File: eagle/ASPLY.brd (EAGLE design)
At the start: 118 x 89 mm, 69 parts, among them IC1 MC78L05ABP, IC2 TINY45, K1 Light, K2 Fan1, K3 Fan2, K4 Fan3, P1 MOLEX, T1 2SC1815, T2 2SC1815, T3 2SC1815, T4 2SC1815

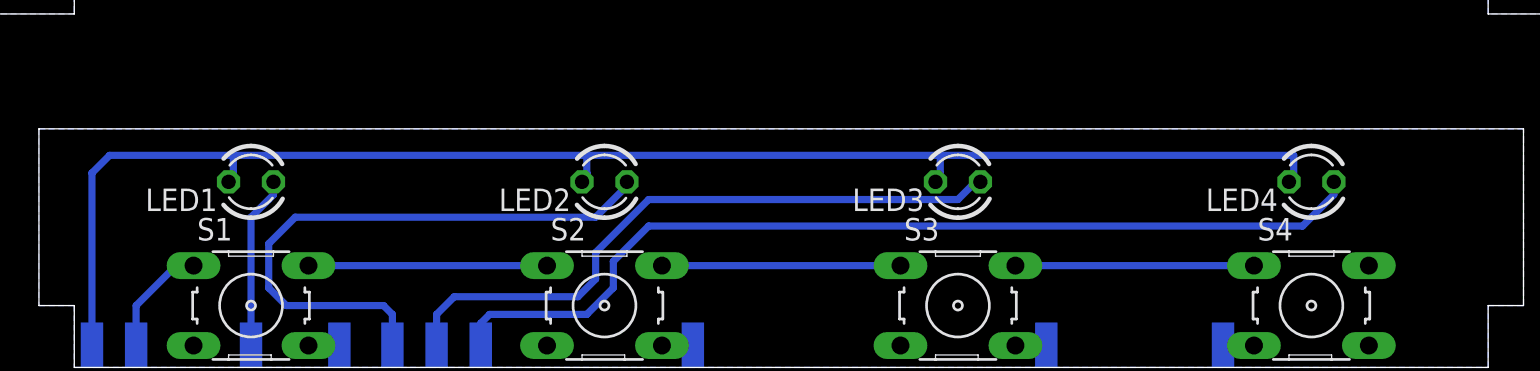
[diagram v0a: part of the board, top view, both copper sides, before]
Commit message: fix schema
The connection of emitter and collector are fixed. Increase in current
limiting resistors of transistors from 2 to 10 kOm
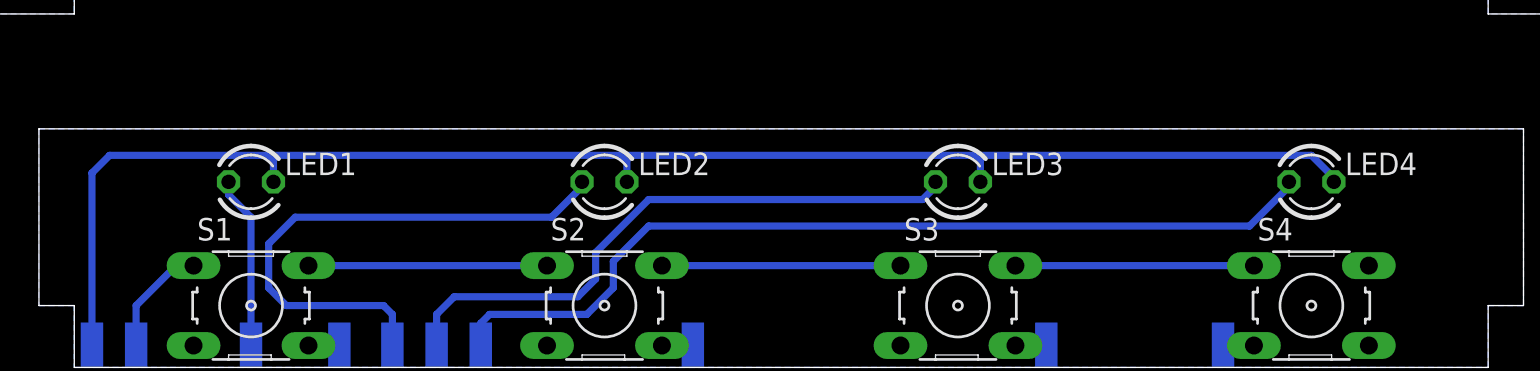
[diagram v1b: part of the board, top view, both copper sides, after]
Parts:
- turned LED1 to 0 degrees
- turned LED2 to 0 degrees
- turned LED3 to 0 degrees
- turned LED4 to 0 degrees
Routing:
- net N$25: track 54.4 -> 51.6 mm
- net N$27: track 33.7 -> 31.2 mm
- net N$26: track 36.5 -> 34.1 mm
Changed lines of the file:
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@@
 <layer number="17" name="Pads" color="2" fill="1" visible="yes" active="yes"/>
 <layer number="18" name="Vias" color="2" fill="1" visible="no" active="yes"/>
-<layer number="19" name="Unrouted" color="6" fill="1" visible="no" active="yes"/>
+<layer number="19" name="Unrouted" color="6" fill="1" visible="yes" active="yes"/>
 <layer number="20" name="Dimension" color="15" fill="1" visible="yes" active="yes"/>
 <layer number="21" name="tPlace" color="7" fill="1" visible="yes" active="yes"/>
 <layer number="22" name="bPlace" color="7" fill="1" visible="no" active="yes"/>
-<layer number="23" name="tOrigins" color="15" fill="1" visible="no" active="yes"/>
+<layer number="23" name="tOrigins" color="15" fill="1" visible="yes" active="yes"/>
 <layer number="24" name="bOrigins" color="15" fill="1" visible="no" active="yes"/>
-<layer number="25" name="tNames" color="7" fill="1" visible="yes" active="yes"/>
+<layer number="25" name="tNames" color="7" fill="1" visible="no" active="yes"/>
 <layer number="26" name="bNames" color="7" fill="1" visible="no" active="yes"/>
-<layer number="27" name="tValues" color="7" fill="1" visible="yes" active="yes"/>
+<layer number="27" name="tValues" color="7" fill="1" visible="no" active="yes"/>
 <layer number="28" name="bValues" color="7" fill="1" visible="no" active="yes"/>
 <layer number="29" name="tStop" color="7" fill="3" visible="no" active="yes"/>
@@
 <layer number="48" name="Document" color="7" fill="1" visible="no" active="yes"/>
 <layer number="49" name="Reference" color="7" fill="1" visible="no" active="yes"/>
-<layer number="51" name="tDocu" color="7" fill="1" visible="yes" active="yes"/>
+<layer number="51" name="tDocu" color="7" fill="1" visible="no" active="yes"/>
 <layer number="52" name="bDocu" color="7" fill="1" visible="no" active="yes"/>
 <layer number="91" name="Nets" color="2" fill="1" visible="no" active="no"/>
@@
 <attribute name="VALUE" x="65.365" y="17.54" size="1.27" layer="27" rot="R90"/>
 </element>
-<element name="LED1" library="led" package="LED3MM" value="Red" x="29" y="-9.5" rot="R180"/>
-<element name="LED2" library="led" package="LED3MM" value="Green" x="49" y="-9.5" rot="R180"/>
-<element name="LED3" library="led" package="LED3MM" value="Green" x="69" y="-9.5" rot="R180"/>
-<element name="LED4" library="led" package="LED3MM" value="Green" x="89" y="-9.5" rot="R180"/>
+<element name="LED1" library="led" package="LED3MM" value="Red" x="29" y="-9.5"/>
+<element name="LED2" library="led" package="LED3MM" value="Green" x="49" y="-9.5"/>
+<element name="LED3" library="led" package="LED3MM" value="Green" x="69" y="-9.5"/>
+<element name="LED4" library="led" package="LED3MM" value="Green" x="89" y="-9.5"/>
 <element name="S1" library="switch-omron" package="B3F-10XX" value="Light" x="29" y="-16.5" smashed="yes">
 <attribute name="OC_NEWARK" value="36M3542" x="29" y="-16.5" size="1.778" layer="27" display="off"/>
@@
 <contactref element="LED4" pad="A"/>
 <contactref element="U$14" pad="P$1"/>
-<wire x1="90.27" y1="-9.5" x2="90.27" y2="-10.23" width="0.4064" layer="16"/>
-<wire x1="90.27" y1="-10.23" x2="88.5" y2="-12" width="0.4064" layer="16"/>
-<wire x1="88.5" y1="-12" x2="51.5" y2="-12" width="0.4064" layer="16"/>
+<wire x1="85.5" y1="-12" x2="51.5" y2="-12" width="0.4064" layer="16"/>
 <wire x1="51.5" y1="-12" x2="49.5" y2="-14" width="0.4064" layer="16"/>
 <wire x1="49.5" y1="-14" x2="49.5" y2="-15.5" width="0.4064" layer="16"/>
@@
 <wire x1="42" y1="-17.5" x2="42" y2="-18.73" width="0.4064" layer="16"/>
 <wire x1="42" y1="-18.73" x2="42" y2="-19" width="0.4064" layer="16"/>
+<wire x1="87.73" y1="-9.5" x2="87.73" y2="-9.77" width="0.4064" layer="16"/>
+<wire x1="87.73" y1="-9.77" x2="85.5" y2="-12" width="0.4064" layer="16"/>
 </signal>
 <signal name="N$26">
 <contactref element="LED3" pad="A"/>
 <contactref element="U$16" pad="P$1"/>
-<wire x1="70.27" y1="-9.5" x2="70" y2="-9.5" width="0.4064" layer="16"/>
-<wire x1="70" y1="-9.5" x2="69" y2="-10.5" width="0.4064" layer="16"/>
-<wire x1="69" y1="-10.5" x2="51.5" y2="-10.5" width="0.4064" layer="16"/>
+<wire x1="67" y1="-10.5" x2="51.5" y2="-10.5" width="0.4064" layer="16"/>
 <wire x1="51.5" y1="-10.5" x2="48.5" y2="-13.5" width="0.4064" layer="16"/>
 <wire x1="48.5" y1="-13.5" x2="48.5" y2="-15" width="0.4064" layer="16"/>
@@
 <wire x1="40.5" y1="-16" x2="39.5" y2="-17" width="0.4064" layer="16"/>
 <wire x1="39.5" y1="-17" x2="39.5" y2="-18.73" width="0.4064" layer="16"/>
+<wire x1="67.73" y1="-9.5" x2="67.73" y2="-9.77" width="0.4064" layer="16"/>
+<wire x1="67.73" y1="-9.77" x2="67" y2="-10.5" width="0.4064" layer="16"/>
 </signal>
 <signal name="N$27">
 <contactref element="LED2" pad="A"/>
 <contactref element="U$18" pad="P$1"/>
-<wire x1="50.27" y1="-9.5" x2="50.27" y2="-9.73" width="0.4064" layer="16"/>
-<wire x1="50.27" y1="-9.73" x2="48.5" y2="-11.5" width="0.4064" layer="16"/>
-<wire x1="48.5" y1="-11.5" x2="31.5" y2="-11.5" width="0.4064" layer="16"/>
+<wire x1="46" y1="-11.5" x2="31.5" y2="-11.5" width="0.4064" layer="16"/>
 <wire x1="31.5" y1="-11.5" x2="30" y2="-13" width="0.4064" layer="16"/>
 <wire x1="30" y1="-13" x2="30" y2="-15.5" width="0.4064" layer="16"/>
@@
 <wire x1="36.5" y1="-16.5" x2="37" y2="-17" width="0.4064" layer="16"/>
 <wire x1="37" y1="-17" x2="37" y2="-18.73" width="0.4064" layer="16"/>
+<wire x1="47.73" y1="-9.5" x2="47.73" y2="-9.77" width="0.4064" layer="16"/>
+<wire x1="47.73" y1="-9.77" x2="46" y2="-11.5" width="0.4064" layer="16"/>
 </signal>
 <signal name="N$28">
 <contactref element="LED1" pad="A"/>
 <contactref element="U$20" pad="P$1"/>
-<wire x1="30.27" y1="-9.5" x2="30.27" y2="-10.23" width="0.4064" layer="16"/>
-<wire x1="30.27" y1="-10.23" x2="29" y2="-11.5" width="0.4064" layer="16"/>
 <wire x1="29" y1="-11.5" x2="29" y2="-18.73" width="0.4064" layer="16"/>
+<wire x1="27.73" y1="-9.5" x2="27.73" y2="-10.23" width="0.4064" layer="16"/>
+<wire x1="27.73" y1="-10.23" x2="29" y2="-11.5" width="0.4064" layer="16"/>
 </signal>
 <signal name="N$44">
@@
 <wire x1="20" y1="-18.73" x2="20" y2="-9" width="0.4064" layer="16"/>
 <wire x1="20" y1="-9" x2="21" y2="-8" width="0.4064" layer="16"/>
-<wire x1="21" y1="-8" x2="28" y2="-8" width="0.4064" layer="16"/>
-<wire x1="28" y1="-9" x2="28" y2="-9.23" width="0.4064" layer="16"/>
-<wire x1="28" y1="-9.23" x2="27.73" y2="-9.5" width="0.4064" layer="16"/>
-<wire x1="27.73" y1="-9.5" x2="27.73" y2="-9.27" width="0.4064" layer="16"/>
-<wire x1="27.73" y1="-9.27" x2="28" y2="-9" width="0.4064" layer="16"/>
-<wire x1="28" y1="-9" x2="28" y2="-8" width="0.4064" layer="16"/>
-<wire x1="28" y1="-8" x2="48" y2="-8" width="0.4064" layer="16"/>
-<wire x1="48" y1="-9" x2="48" y2="-9.23" width="0.4064" layer="16"/>
-<wire x1="48" y1="-9.23" x2="47.73" y2="-9.5" width="0.4064" layer="16"/>
-<wire x1="47.73" y1="-9.5" x2="47.73" y2="-9.27" width="0.4064" layer="16"/>
-<wire x1="47.73" y1="-9.27" x2="48" y2="-9" width="0.4064" layer="16"/>
-<wire x1="48" y1="-9" x2="48" y2="-8" width="0.4064" layer="16"/>
-<wire x1="48" y1="-8" x2="68" y2="-8" width="0.4064" layer="16"/>
-<wire x1="68" y1="-9" x2="68" y2="-9.23" width="0.4064" layer="16"/>
-<wire x1="68" y1="-9.23" x2="67.73" y2="-9.5" width="0.4064" layer="16"/>
-<wire x1="67.73" y1="-9.5" x2="67.73" y2="-9.27" width="0.4064" layer="16"/>
-<wire x1="67.73" y1="-9.27" x2="68" y2="-9" width="0.4064" layer="16"/>
-<wire x1="68" y1="-9" x2="68" y2="-8" width="0.4064" layer="16"/>
-<wire x1="68" y1="-8" x2="88" y2="-8" width="0.4064" layer="16"/>
-<wire x1="88" y1="-8" x2="88" y2="-9.23" width="0.4064" layer="16"/>
-<wire x1="88" y1="-9.23" x2="87.73" y2="-9.5" width="0.4064" layer="16"/>
+<wire x1="21" y1="-8" x2="30" y2="-8" width="0.4064" layer="16"/>
+<wire x1="30" y1="-8" x2="50" y2="-8" width="0.4064" layer="16"/>
+<wire x1="50" y1="-8" x2="70" y2="-8" width="0.4064" layer="16"/>
+<wire x1="70" y1="-8" x2="89" y2="-8" width="0.4064" layer="16"/>
+<wire x1="90.27" y1="-9.5" x2="90.27" y2="-9.27" width="0.4064" layer="16"/>
+<wire x1="90.27" y1="-9.27" x2="89" y2="-8" width="0.4064" layer="16"/>
+<wire x1="70.27" y1="-9.5" x2="70.27" y2="-8.27" width="0.4064" layer="16"/>
+<wire x1="70.27" y1="-8.27" x2="70" y2="-8" width="0.4064" layer="16"/>
+<wire x1="50.27" y1="-9.5" x2="50.27" y2="-8.27" width="0.4064" layer="16"/>
+<wire x1="50.27" y1="-8.27" x2="50" y2="-8" width="0.4064" layer="16"/>
+<wire x1="30.27" y1="-9.5" x2="30.27" y2="-8.27" width="0.4064" layer="16"/>
+<wire x1="30.27" y1="-8.27" x2="30" y2="-8" width="0.4064" layer="16"/>
 </signal>
 <signal name="N$24">

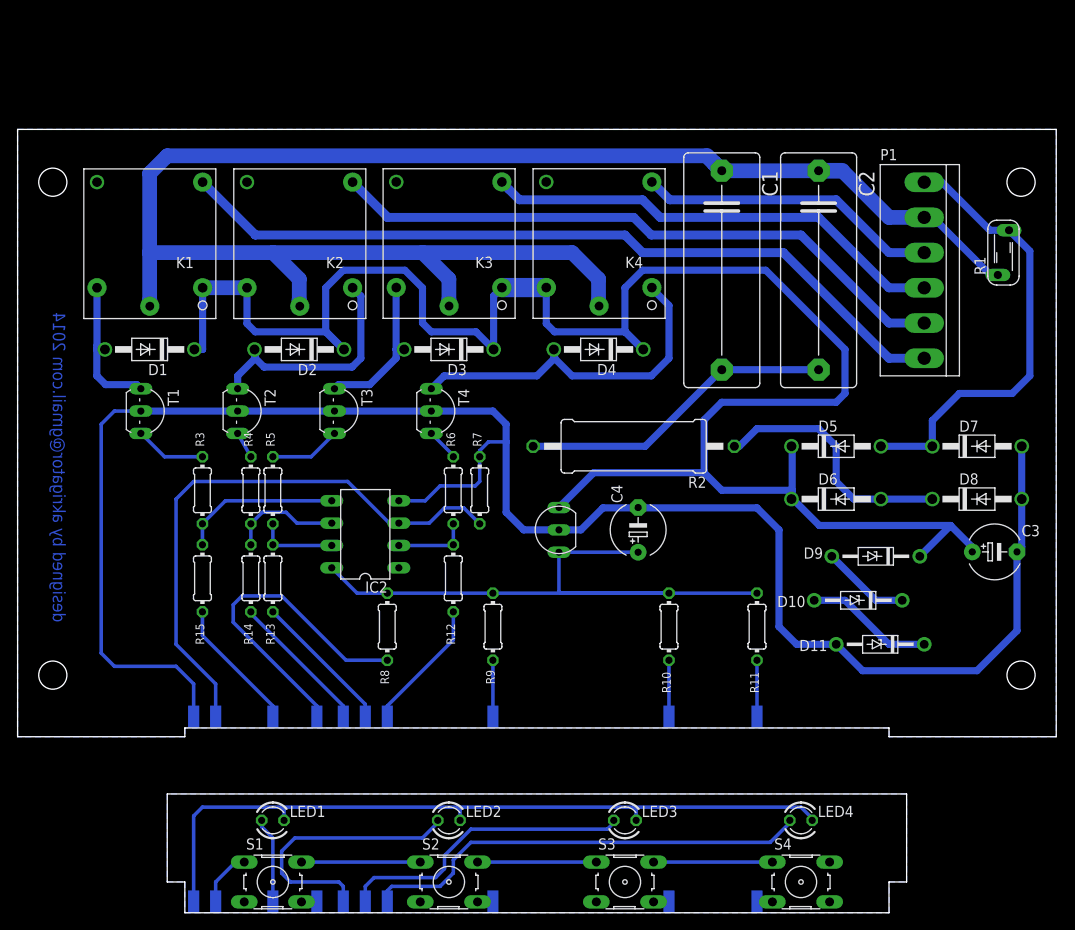
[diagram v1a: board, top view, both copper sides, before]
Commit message: New HW revision:
- Split LED and transistor manage
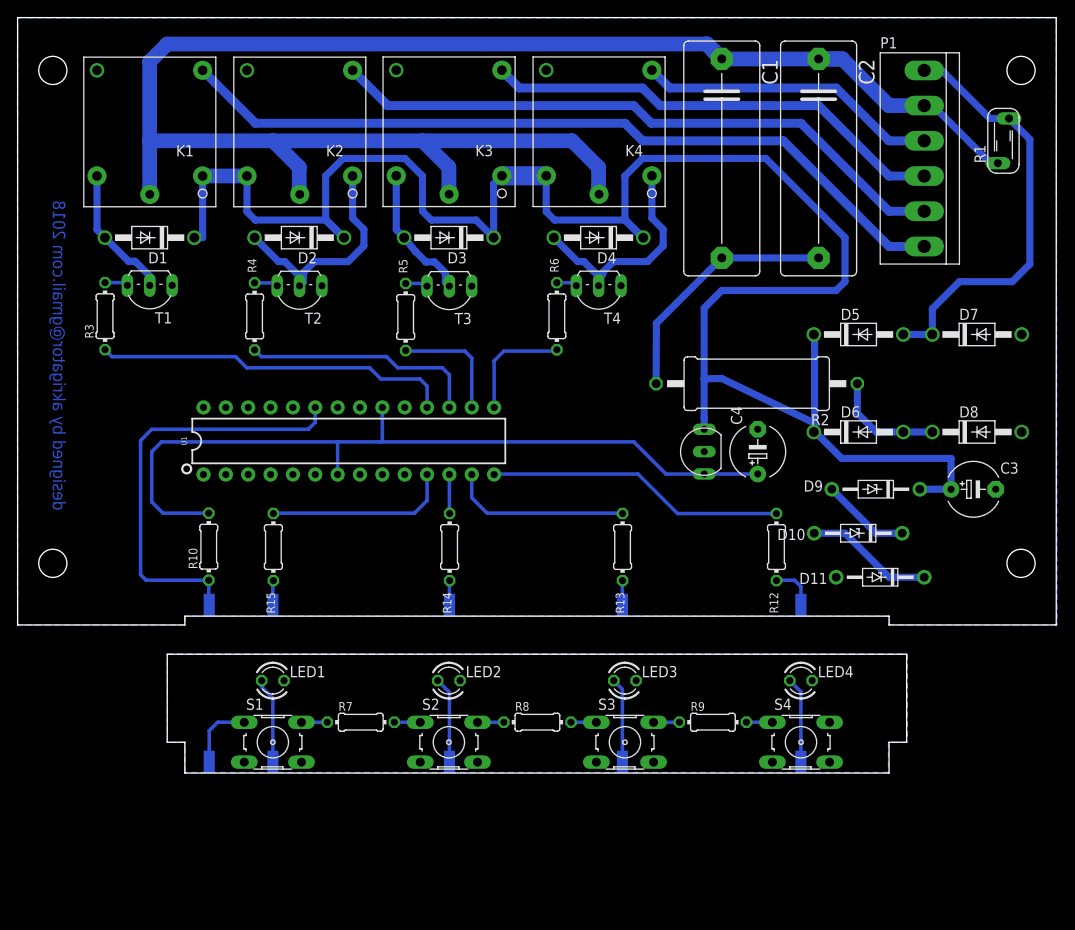
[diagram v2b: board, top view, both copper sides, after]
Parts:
- removed IC2: TINY45, atmel:DIL08
- removed R11: 2k, rcl:0204/7
- removed U$10, U$11, U$12, U$15, U$17, U$19, U$2, U$4, U$6, U$9: PIN, ASPLY:PIN
- added U1: 328P, SparkFun-IC-Microcontroller:DIP28
- R10: value 1k -> 2k
- R3, R4, R5, R6: value 2k -> 5.1k
- R8: value 270 -> 1k
- R9: value 510 -> 1k
- moved U$13 64.2 mm to (21.8, -4.12)
- moved R10 53.1 mm to (21.7, 21.6)
- moved U$14 49.6 mm to (89.0, -4.12)
- moved U$7 48.7 mm to (89.0, 13.7)
- moved R13 39.9 mm to (68.7, 21.5)
- moved R12 36.9 mm to (86.2, 21.5)
- moved U$16 33.2 mm to (68.7, -4.12)
- moved U$5 31.9 mm to (68.7, 13.7)
- moved R7 29.6 mm to (39.0, 1.65), turned to 0 degrees
- moved R9 27.2 mm to (79.0, 1.65), turned to 0 degrees
- moved R5 24.8 mm to (44.1, 47.7)
- moved T4 23.8 mm to (66.0, 51.2), turned to 180 degrees
- moved R6 23.0 mm to (61.3, 47.8)
- moved R14 22.9 mm to (49.1, 21.5)
- moved R3 22.7 mm to (9.94, 47.8)
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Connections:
- net N$1 renamed 220V
- net N$25 renamed LED_FAN3
- net N$26 renamed LED_FAN2
- net N$27 renamed LED_FAN1
- net N$28 renamed LED_LIGHT
- net N$6 renamed 0
- removed net N$29 (its old number): S3.2, S4.1
- removed net N$30: LED1.K, LED2.K, LED3.K, LED4.K, U$11.P$1
- removed net N$31: S1.4, U$19.P$1
- removed net N$32: S2.4, U$17.P$1
- removed net N$33: S3.4, U$15.P$1
- removed net N$34: S4.3, U$13.P$1
- removed net N$35: IC2.3, R7.1, U$9.P$1
- removed net N$37: R11.1, U$2.P$1
- removed net N$39: R10.1, U$4.P$1
- removed net N$41: IC2.2, R12.2, R6.1
- removed net N$44: IC2.5, R15.2, R3.1
- removed net N$45: R9.1, U$6.P$1
- removed net N$47: R8.1, U$8.P$1
- new net BUTTONS_INPUT: R10.1, U$8.P$1, U1.23
- new net LED_FAN1_OUTPUT: R14.2, U1.12
- new net LED_FAN2_OUTPUT: R13.2, U1.13
- new net LED_FAN3_OUTPUT: R12.2, U1.14
- new net LED_LIGHT_OUTPUT: R15.2, U1.11
- new net N$1: S1.1, U$13.P$1
- new net N$15: R7.2, S2.1
- new net N$25: R9.2, S4.1
- new net N$6: R7.1, S1.2
- new net N$7: R6.1, U1.15
- new net N$8: R5.1, U1.16
- net 5V: now also U1.20, U1.7; no longer IC2.8, R11.2, R8.2, R9.2
- net GND: now also LED1.K, LED2.K, LED3.K, LED4.K, S1.3, S1.4, S2.3, S2.4, S3.3, S3.4, S4.3, S4.4, T1.E, T2.E, T3.E, T4.E, U1.22, U1.8; no longer IC2.4, R7.2, T1.C, T2.C, T3.C, T4.C, U$10.P$1
- net N$10: now also T2.C; no longer T2.E
- net N$11: now also T3.C; no longer T3.E
- net N$12: now also T4.C; no longer T4.E
- net N$22: now also R8.1, S2.2; no longer S1.2, S2.1
- net N$23: now also R8.2; no longer S2.2
- net N$24: now also R9.1, S3.2; no longer S1.1, U$12.P$1
- net N$42: now also R4.1, U1.17; no longer IC2.7, R13.2, R5.1
- net N$43: now also R3.1, U1.18; no longer IC2.6, R14.2, R4.1
- net N$9: now also T1.C; no longer T1.E
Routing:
- net GND: track 213.5 -> 0.00 mm
- net N$30: track 86.0 -> 0.00 mm
- net N$35: track 65.3 -> 0.00 mm
- net BUTTONS_INPUT: track 0.00 -> 48.5 mm
- net LED_FAN3: track 51.6 -> 9.75 mm
- net N$47: track 37.9 -> 0.00 mm
- net LED_FAN3_OUTPUT: track 0.00 -> 34.0 mm
- net N$43: track 12.6 -> 40.7 mm
- net LED_FAN2: track 34.1 -> 9.64 mm
- net LED_FAN1: track 31.2 -> 9.78 mm
- net LED_LIGHT_OUTPUT: track 0.00 -> 21.0 mm
- net LED_FAN2_OUTPUT: track 0.00 -> 20.5 mm
- net N$44: track 18.2 -> 0.00 mm
- net N$42: track 9.10 -> 27.0 mm
- net 5V: track 75.5 -> 91.2 mm
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- added copper zone on layer 16, net GND
- removed copper zone on layer 16, net N$7
- removed copper zone on layer 16, net N$8
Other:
- board size 118 x 89 mm -> 118 x 85.8 mm
- board text added: "designed by akrigator@gmail.com 2018"
- board text removed: "designed by akrigator@gmail.com 2014"

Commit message: Setup power supply
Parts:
- C1, C2: value 0.33uF 275VAC -> 1uF 275VAC
- R12, R13, R14, R15: value 220 -> 1k
- R2: value 220 -> 100
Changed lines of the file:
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@@
 <element name="D7" library="diode" package="DO41-10" value="1N4007" x="109" y="45.7"/>
 <element name="D8" library="diode" package="DO41-10" value="1N4007" x="109" y="34.62"/>
-<element name="C1" library="capacitor-wima" package="C22.5B8" value="0.33uF 275VAC" x="80" y="65.7" smashed="yes" rot="R270">
+<element name="C1" library="capacitor-wima" package="C22.5B8" value="1uF 275VAC" x="80" y="65.7" smashed="yes" rot="R270">
 <attribute name="NAME" x="84.572" y="77.003" size="1.778" layer="25" ratio="10" rot="R270"/>
 <attribute name="VALUE" x="76.96" y="72.78" size="1.778" layer="27" ratio="10" rot="R270"/>
 </element>
-<element name="C2" library="capacitor-wima" package="C22.5B8" value="0.33uF 275VAC" x="91" y="65.7" smashed="yes" rot="R270">
+<element name="C2" library="capacitor-wima" package="C22.5B8" value="1uF 275VAC" x="91" y="65.7" smashed="yes" rot="R270">
 <attribute name="NAME" x="95.572" y="77.003" size="1.778" layer="25" ratio="10" rot="R270"/>
 <attribute name="VALUE" x="87.96" y="72.78" size="1.778" layer="27" ratio="10" rot="R270"/>
 </element>
-<element name="R2" library="resistor" package="0617/22" value="220" x="83.97" y="40.112" rot="R180"/>
+<element name="R2" library="resistor" package="0617/22" value="100" x="83.97" y="40.112" rot="R180"/>
 <element name="C3" library="rcl" package="E5-6" value="47uF 50V" x="108.587" y="28.112" smashed="yes">
 <attribute name="NAME" x="111.635" y="29.89" size="1.27" layer="25" ratio="10"/>
@@
 <attribute name="VALUE" x="61.7476" y="46.1464" size="0.9906" layer="27" ratio="10" rot="R90"/>
 </element>
-<element name="R12" library="rcl" package="0204/7" value="220" x="86.215" y="21.549" smashed="yes" rot="R90">
+<element name="R12" library="rcl" package="0204/7" value="1k" x="86.215" y="21.549" smashed="yes" rot="R90">
 <attribute name="NAME" x="86.4196" y="14.009" size="0.9906" layer="25" ratio="10" rot="R90"/>
 <attribute name="VALUE" x="86.6976" y="19.9234" size="0.9906" layer="27" ratio="10" rot="R90"/>
 </element>
-<element name="R13" library="rcl" package="0204/7" value="220" x="68.729" y="21.549" smashed="yes" rot="R90">
+<element name="R13" library="rcl" package="0204/7" value="1k" x="68.729" y="21.549" smashed="yes" rot="R90">
 <attribute name="NAME" x="68.9336" y="14.009" size="0.9906" layer="25" ratio="10" rot="R90"/>
 <attribute name="VALUE" x="69.2116" y="19.9234" size="0.9906" layer="27" ratio="10" rot="R90"/>
 </element>
-<element name="R14" library="rcl" package="0204/7" value="220" x="49.084" y="21.549" smashed="yes" rot="R90">
+<element name="R14" library="rcl" package="0204/7" value="1k" x="49.084" y="21.549" smashed="yes" rot="R90">
 <attribute name="NAME" x="49.2886" y="14.009" size="0.9906" layer="25" ratio="10" rot="R90"/>
 <attribute name="VALUE" x="49.5666" y="19.9234" size="0.9906" layer="27" ratio="10" rot="R90"/>
 </element>
-<element name="R15" library="rcl" package="0204/7" value="220" x="29.058" y="21.549" smashed="yes" rot="R90">
+<element name="R15" library="rcl" package="0204/7" value="1k" x="29.058" y="21.549" smashed="yes" rot="R90">
 <attribute name="NAME" x="29.2626" y="14.009" size="0.9906" layer="25" ratio="10" rot="R90"/>
 <attribute name="VALUE" x="29.5406" y="19.9234" size="0.9906" layer="27" ratio="10" rot="R90"/>
